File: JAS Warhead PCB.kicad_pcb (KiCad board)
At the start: 2 copper layers, 70 x 65.7 mm, 62 parts, among them J3 Conn_01x02_Socket, J4 Conn_01x02_Socket, J5 Conn_01x02_Socket, J6 Conn_01x02_Socket, J7 Conn_01x02_Socket, J8 Conn_01x15_Socket, J9 Conn_01x15_Socket, U1 LM7805_TO220, U10 AP2127R-3.3, U2 AP2127R-3.3, U3 AP2127R-3.3, U5 MAX31855KASA, U6 MAX31855KASA, U7 MAX31855KASA, U8 AP2127R-3.3, U9 MAX31855KASA

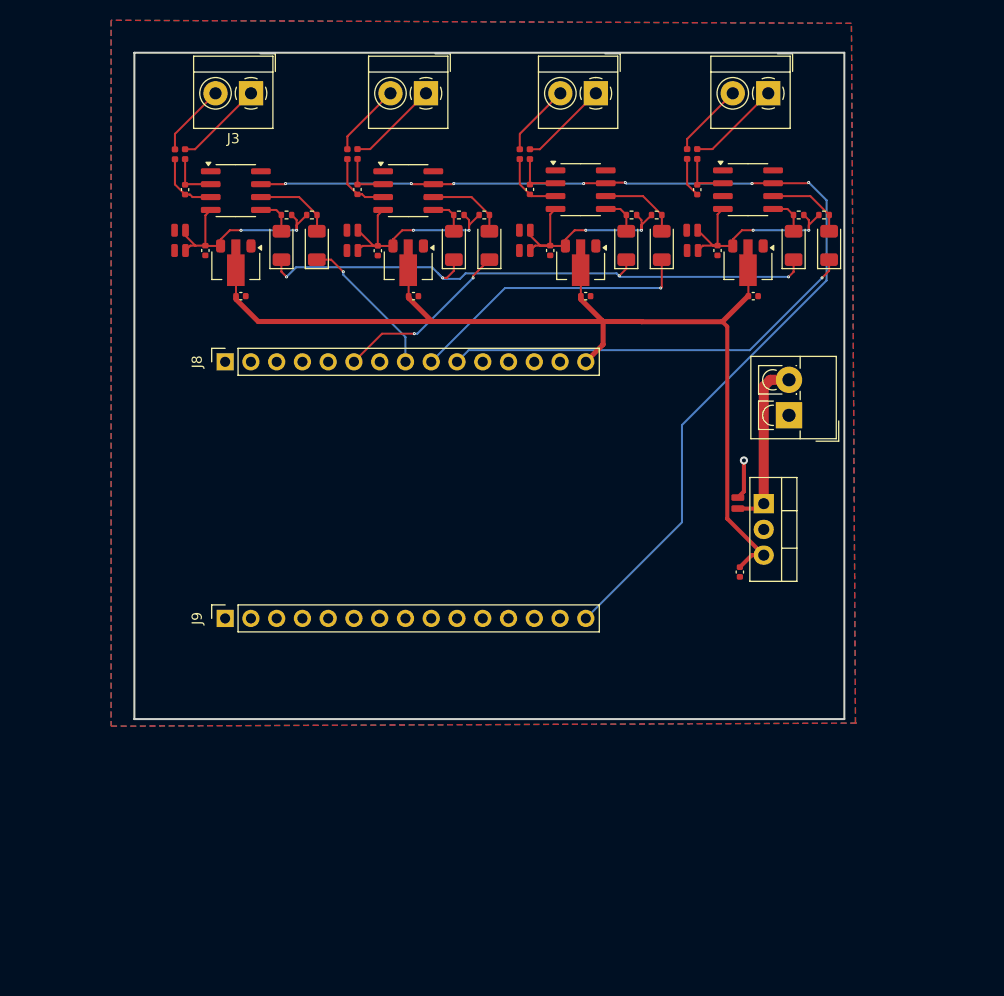
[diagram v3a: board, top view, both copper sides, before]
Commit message: mounting holes
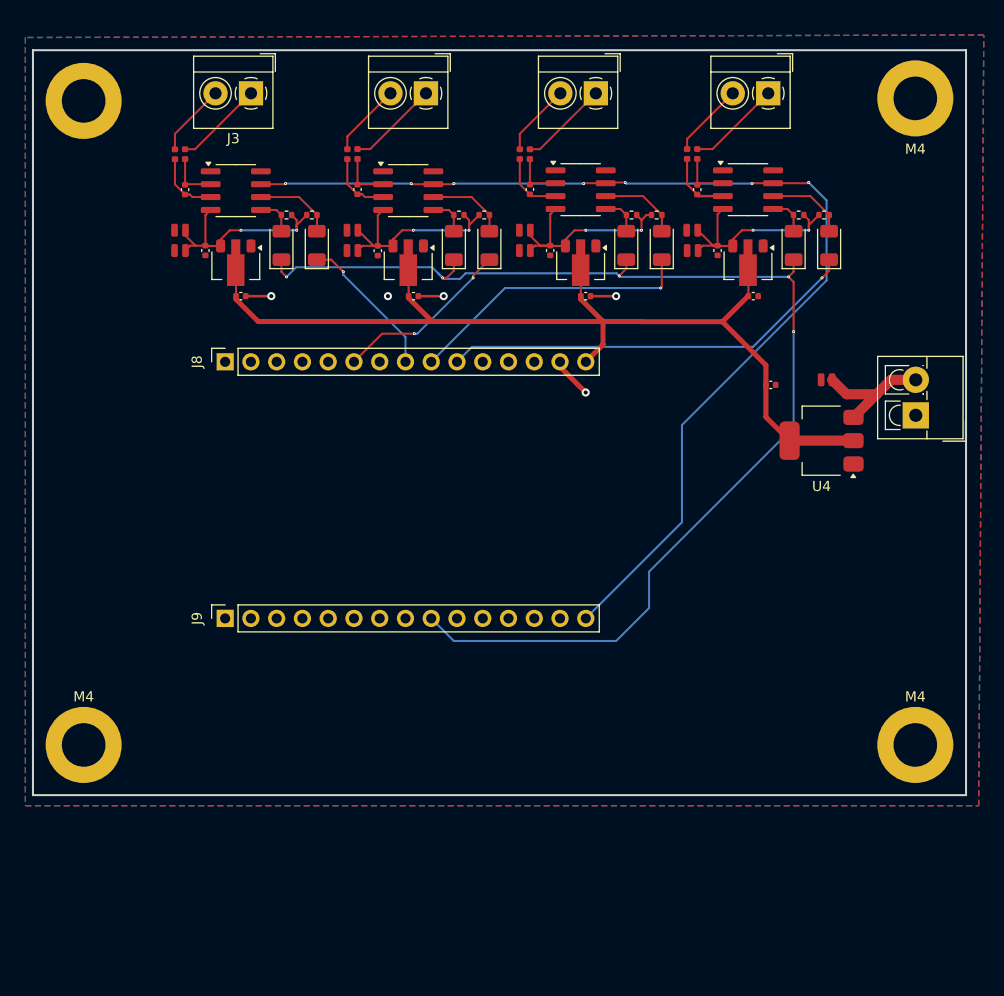
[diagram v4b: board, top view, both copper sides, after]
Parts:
- removed U1: LM7805_TO220, Package_TO_SOT_THT:TO-220-3_Vertical
- added H1: MountingHole_Pad, MountingHole:MountingHole_4.3mm_M4_DIN965_Pad, F.Cu at (95.0, 54.8)
- added M4: MountingHole_Pad, MountingHole:MountingHole_4.3mm_M4_DIN965_Pad, F.Cu at (177.0, 118.2)
- added M4: MountingHole_Pad, MountingHole:MountingHole_4.3mm_M4_DIN965_Pad, F.Cu at (177.0, 54.5)
- added M4: MountingHole_Pad, MountingHole:MountingHole_4.3mm_M4_DIN965_Pad, F.Cu at (95.0, 118.2)
- added U4: LD1117S50TR_SOT223, Package_TO_SOT_SMD:SOT-223-3_TabPin2, F.Cu at (167.8, 88.2)
- moved C2 18.7 mm to (162.8, 82.8), turned to 0 degrees
- moved C1 15.0 mm to (168.2, 82.2), turned to 180 degrees
- moved J7 12.5 mm to (177.0, 85.8)
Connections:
- net /ESP32 Headers/3.3V renamed +3.3V
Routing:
- net /SPI CLK: track 59.6 -> 122.1 mm, vias 4 -> 5
- net GND: track 3.91 -> 11.6 mm, vias 1 -> 5
- net +5V: track 111.3 -> 104.5 mm
- net +12V: track 17.1 -> 12.7 mm
- net Net-(U7-T+): track 3.92 -> 6.51 mm
- net +3V3: track 89.6 -> 88.8 mm
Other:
- board size 70 x 65.7 mm -> 92 x 73.5 mm

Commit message: relays
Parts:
- added D1: 1N4001, Diode_THT:D_DO-41_SOD81_P10.16mm_Horizontal, F.Cu at (129.3, 118.5)
- added D10: 1N4001, Diode_THT:D_DO-41_SOD81_P10.16mm_Horizontal, F.Cu at (142.4, 118.2)
- added J1: Conn_01x02_Socket, TerminalBlock_4Ucon:TerminalBlock_4Ucon_1x02_P3.50mm_Vertical, F.Cu at (175.5, 134.2)
- added J2: Conn_01x02_Socket, TerminalBlock_4Ucon:TerminalBlock_4Ucon_1x02_P3.50mm_Vertical, F.Cu at (93.0, 134.3)
- added K1: Panasonic_ALFG1PF12, Relay_THT:Relay_SPDT_Omron_G2RL-1-E, F.Cu at (126.3, 129.3)
- added K2: Panasonic_ALFG1PF12, Relay_THT:Relay_SPDT_Omron_G2RL-1-E, F.Cu at (145.7, 136.7)
- added Q1: PN2222A, Package_TO_SOT_THT:TO-92_Inline, F.Cu at (167.7, 122.8)
- added Q2: PN2222A, Package_TO_SOT_THT:TO-92_Inline, F.Cu at (101.5, 122.8)
- added R1: 4.7K, Resistor_SMD:R_0815_2038Metric, F.Cu at (109.0, 122.5)
- added R10: 50K, Resistor_SMD:R_2816_7142Metric_Pad3.20x4.45mm_HandSolder, F.Cu at (124.3, 123.8)
- added R11: 50K, Resistor_SMD:R_2816_7142Metric_Pad3.20x4.45mm_HandSolder, F.Cu at (147.9, 123.8)
- added R12: 4.7K, Resistor_SMD:R_0815_2038Metric, F.Cu at (163.2, 122.5)
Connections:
- J9 pad 5: /ESP32 Headers/D4 -> /RELAY1
- J9 pad 8: /ESP32 Headers/D5 -> /RELAY2
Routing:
- net +12V: track 12.7 -> 161.8 mm
- net /RELAY2: track 0.00 -> 43.7 mm, vias 0 -> 1
- net Net-(J1-Pin_2): track 0.00 -> 25.0 mm
- net Net-(D10-K): track 0.00 -> 21.0 mm
- net Net-(J2-Pin_2): track 0.00 -> 20.8 mm
- net Net-(D1-A): track 0.00 -> 20.8 mm, vias 0 -> 1
- net /RELAY1: track 0.00 -> 20.5 mm, vias 0 -> 1
- net Net-(D1-K): track 0.00 -> 18.7 mm, vias 0 -> 1
- net Net-(D10-A): track 0.00 -> 18.0 mm
- net Net-(K1-PadA2): track 0.00 -> 14.5 mm
- net Net-(Q2-B): track 0.00 -> 8.83 mm, vias 0 -> 1
- net Net-(Q1-B): track 0.00 -> 6.42 mm
- net Net-(K2-PadA2): track 0.00 -> 5.61 mm
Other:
- board size 92 x 73.5 mm -> 92 x 89.9 mm
- board text added: "M4"
- board text added: "OIL PUMP"
- board text added: "WTR PUMP"

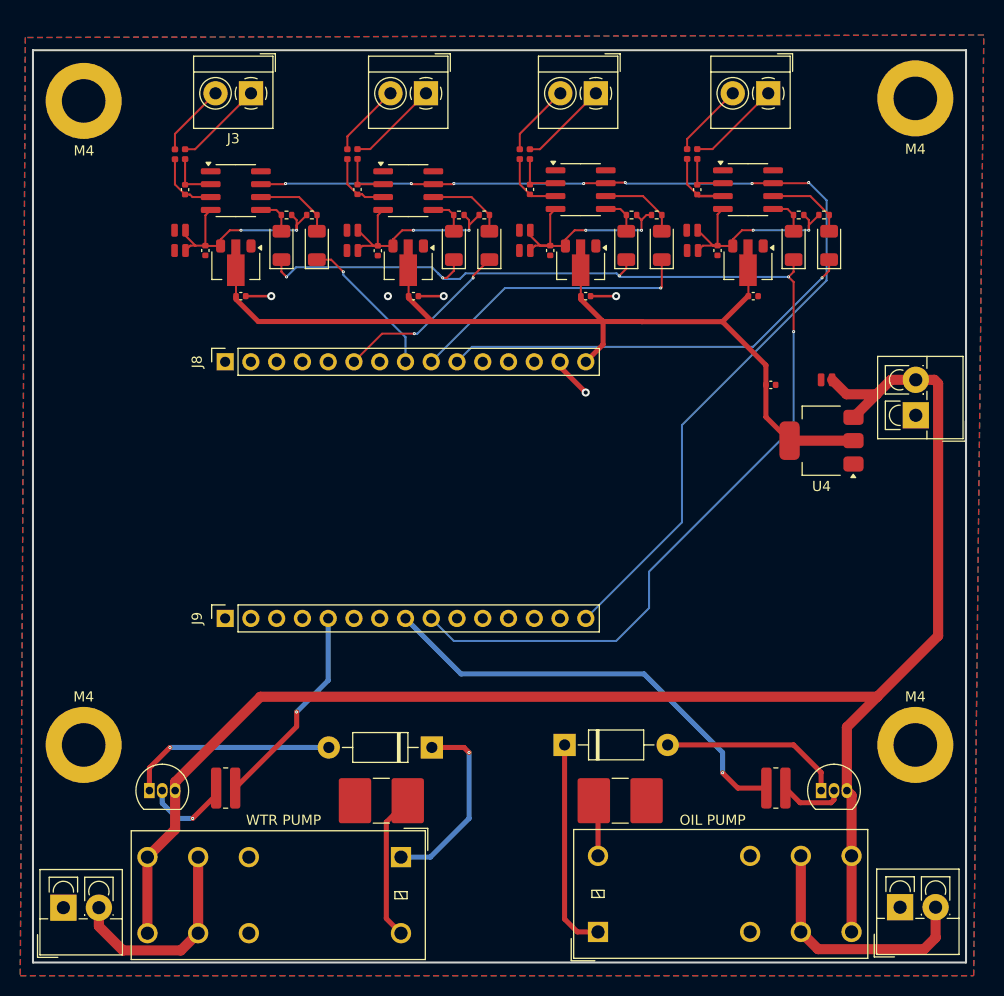
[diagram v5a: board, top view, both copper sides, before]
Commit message: adds thermister locations
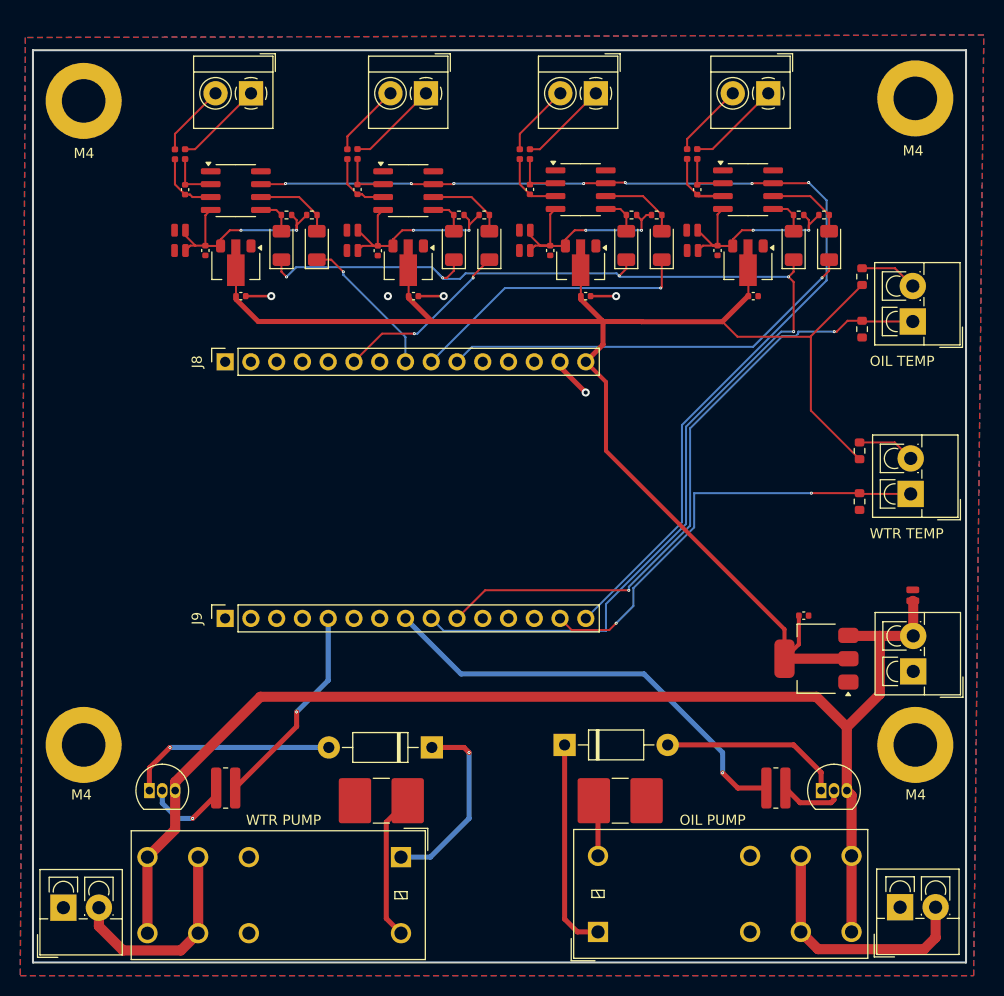
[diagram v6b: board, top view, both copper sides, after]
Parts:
- added J10: Conn_01x02_Socket, TerminalBlock_4Ucon:TerminalBlock_4Ucon_1x02_P3.50mm_Vertical, F.Cu at (176.8, 76.5)
- added J11: Conn_01x02_Socket, TerminalBlock_4Ucon:TerminalBlock_4Ucon_1x02_P3.50mm_Vertical, F.Cu at (176.5, 93.5)
- added R13: 100K, Resistor_SMD:R_0603_1608Metric, F.Cu at (171.8, 77.2)
- added R14: 100K, Resistor_SMD:R_0603_1608Metric, F.Cu at (171.8, 72.1)
- added R15: 100K, Resistor_SMD:R_0603_1608Metric, F.Cu at (171.5, 89.2)
- added R16: 100K, Resistor_SMD:R_0603_1608Metric, F.Cu at (171.5, 94.2)
- moved J7 25.3 mm to (176.8, 111.0)
- moved C2 23.0 mm to (166.0, 105.5)
- moved C1 22.9 mm to (176.8, 103.5), turned to 90 degrees
- moved U4 21.5 mm to (167.2, 109.8)
- renumbered M4 to H2, M4 to H3, M4 to H4
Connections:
- J9 pad 10: /ESP32 Headers/D19 -> /OilTemp
- J9 pad 14: /ESP32 Headers/D22 -> /WtrTemp
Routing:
- net /OilTemp: track 0.00 -> 63.0 mm, vias 0 -> 2
- net +5V: track 104.5 -> 162.9 mm
- net /WtrTemp: track 0.00 -> 43.7 mm, vias 0 -> 2
- net +12V: track 161.8 -> 127.6 mm
- net Net-(J10-Pin_2): track 0.00 -> 5.72 mm
- net Net-(J11-Pin_2): track 0.00 -> 5.70 mm
- net /SPI CLK: track 122.1 -> 120.8 mm
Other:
- board text added: "OIL TEMP"
- board text added: "WTR TEMP"

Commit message: adds graphics
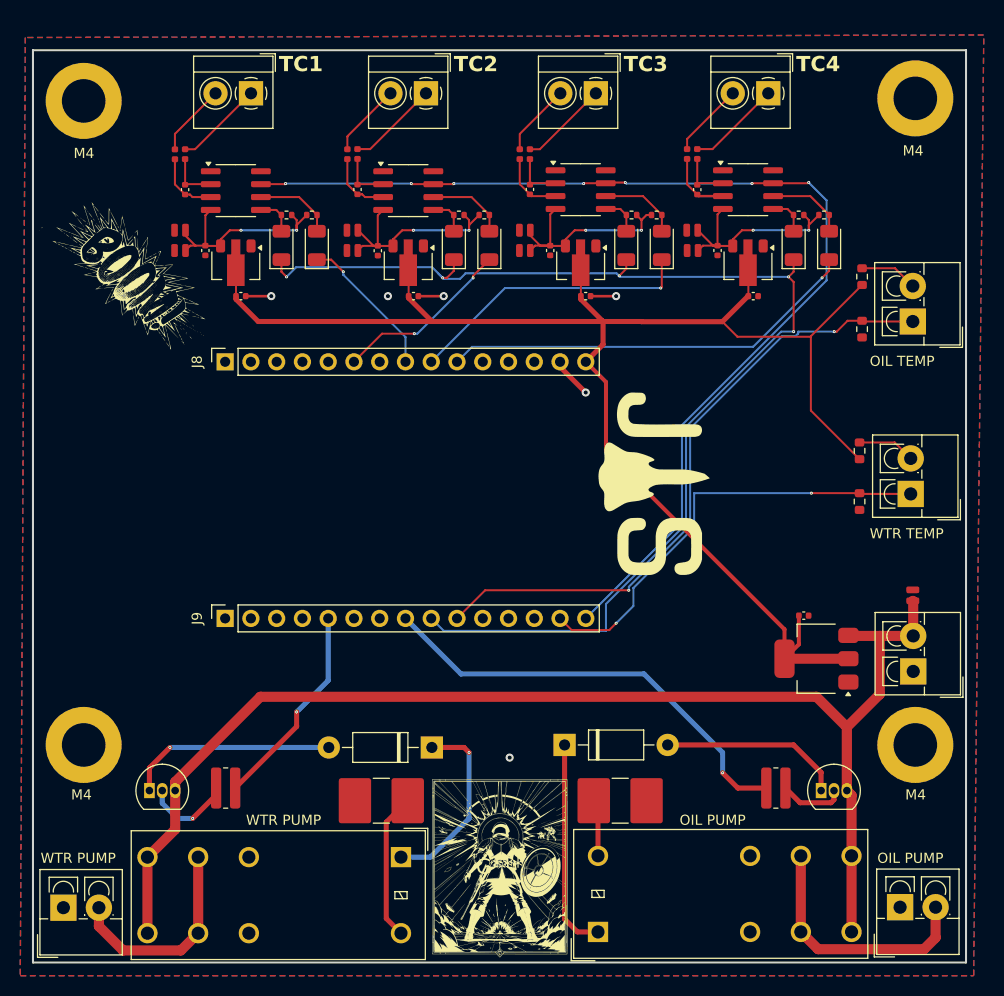
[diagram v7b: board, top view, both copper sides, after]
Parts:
- added G***: LOGO, LOGO, F.Cu at (136.0, 130.2)
- added G***: LOGO, LOGO, F.Cu at (151.2, 92.5)
- added G***: LOGO, LOGO, F.Cu at (100.0, 72.2)
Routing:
- net GND: vias 5 -> 6
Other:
- board text added: "Peter Cross Matt Aranibar"
- board text added: "TC1"
- board text added: "TC2"
- board text added: "TC3"
- board text added: "TC4"
